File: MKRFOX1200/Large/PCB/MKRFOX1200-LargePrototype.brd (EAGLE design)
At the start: 100 x 100 mm, 195 parts, among them IC2 ARDUINO_MKRFOX1200PROTOPADS, U1 GENERIC-SOIC8, U2 GENERIC-SOIC8, U3 GENERIC-SOIC8, U4 GENERIC-SOIC8

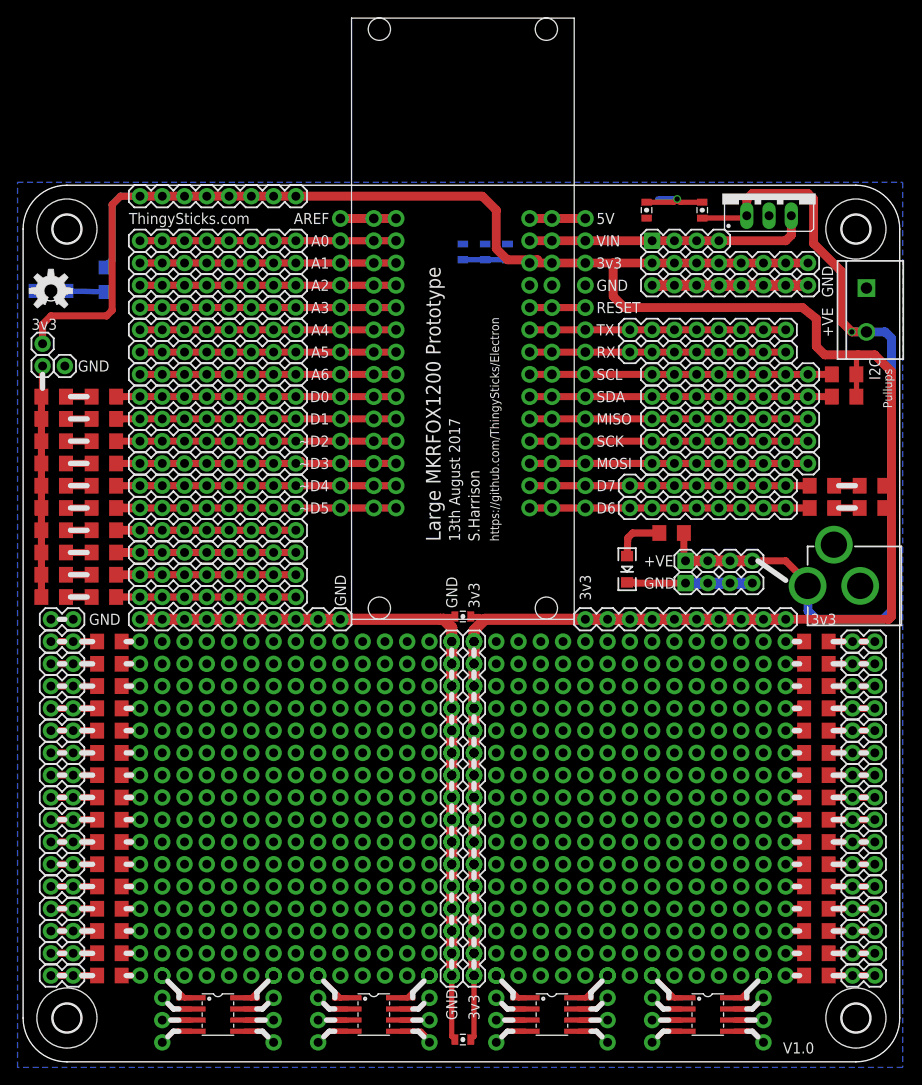
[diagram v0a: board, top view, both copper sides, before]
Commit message: Updated links and name to make it not MKRFox1200 specific as the pinout is the same for WiFi
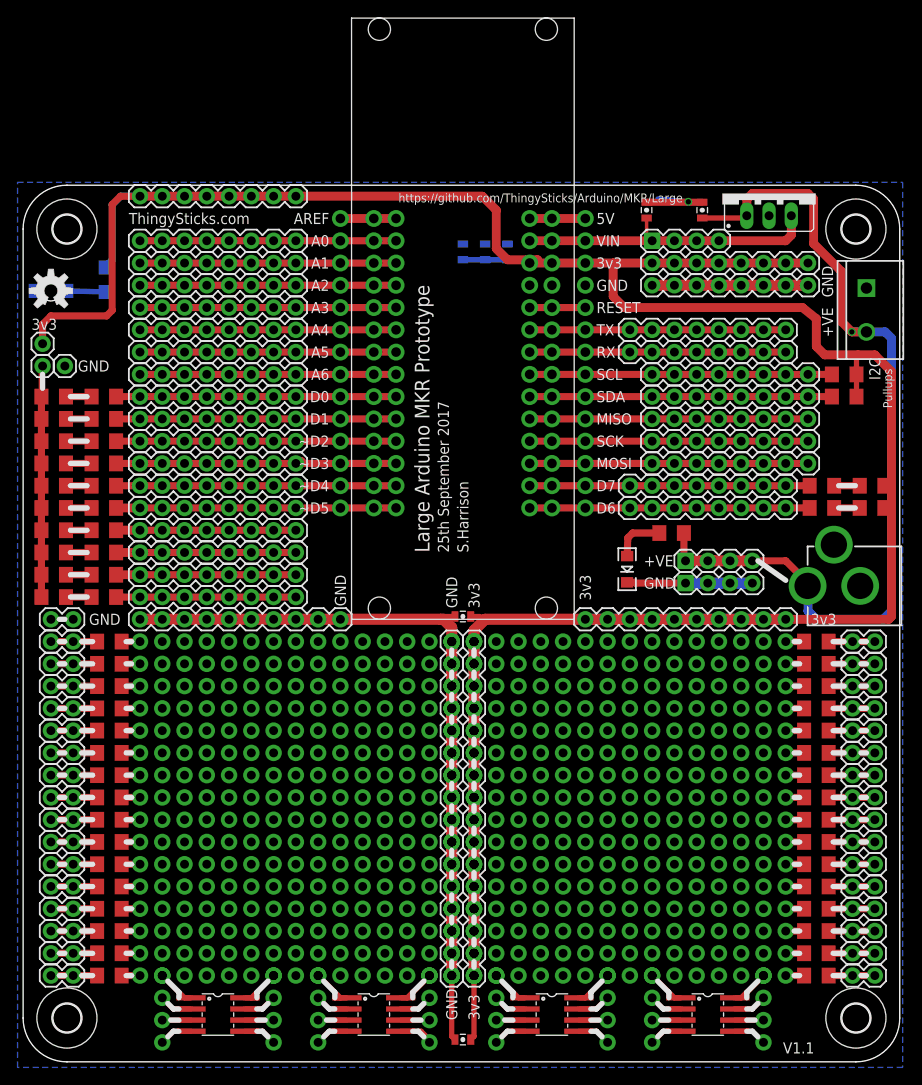
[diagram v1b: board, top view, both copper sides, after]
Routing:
- net GND: track 164.7 -> 167.3 mm
- net VIN: track 32.3 -> 34.9 mm
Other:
- board text added: "25th September 2017"
- board text added: "Large Arduino MKR Prototype"
- board text added: "Large MKR Prototype"
- board text added: "V1.1"
- board text added: "http://ThingySticks.com/Arduino/Prototype/Large"
- board text added: "https://github.com/ThingySticks/Arduino/MKR/Large"
- board text removed: "13th August 2017"
- board text removed: "Large MKRFOX1200 Prototype"
- board text removed: "V1.0"
- board text removed: "https://github.com/ThingySticks/Electron"
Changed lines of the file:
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@@
 <text x="93.0275" y="49.8475" size="1.27" layer="26" font="vector" rot="MR0">3v3</text>
 <text x="12.065" y="95.5675" size="1.27" layer="25" font="vector" ratio="10">ThingySticks.com</text>
-<text x="52.07" y="59.3725" size="1.27" layer="25" font="vector" rot="R90">S.Harrison</text>
-<text x="49.8475" y="59.3725" size="1.27" layer="25" font="vector" rot="R90">13th August 2017</text>
-<text x="47.625" y="59.3725" size="1.6764" layer="25" font="vector" rot="R90">Large MKRFOX1200 Prototype</text>
-<text x="86.6775" y="0.9525" size="1.27" layer="25" font="vector">V1.0</text>
+<text x="50.8" y="58.1025" size="1.27" layer="25" font="vector" rot="R90">S.Harrison</text>
+<text x="48.5775" y="58.1025" size="1.27" layer="25" font="vector" rot="R90">25th September 2017</text>
+<text x="46.355" y="58.1025" size="1.6764" layer="25" font="vector" rot="R90">Large Arduino MKR Prototype</text>
+<text x="86.6775" y="0.9525" size="1.27" layer="25" font="vector">V1.1</text>
 <text x="11.1125" y="51.1175" size="1.27" layer="25" font="vector" rot="R180">GND</text>
 <text x="91.1225" y="86.0425" size="1.27" layer="25" font="vector" rot="R270">+VE</text>
@@
 <wire x1="17.78" y1="7.3025" x2="17.78" y2="7.9375" width="0.6096" layer="25"/>
 <wire x1="17.78" y1="7.9375" x2="16.51" y2="9.2075" width="0.6096" layer="25"/>
-<text x="54.2925" y="59.3725" size="1.016" layer="25" rot="R90">https://github.com/ThingySticks/Electron</text>
+<text x="75.2475" y="99.06" size="1.016" layer="25" rot="R180">https://github.com/ThingySticks/Arduino/MKR/Large</text>
 <wire x1="93.0275" y1="65.7225" x2="94.9325" y2="65.7225" width="0.6096" layer="25"/>
 <wire x1="5.3975" y1="58.1025" x2="7.3025" y2="58.1025" width="0.6096" layer="25"/>
@@
 <wire x1="2.2225" y1="76.835" x2="2.2225" y2="78.4225" width="0.6096" layer="25"/>
 <wire x1="5.3975" y1="55.5625" x2="7.3025" y2="55.5625" width="0.6096" layer="25"/>
-<text x="47.625" y="58.7375" size="1.6764" layer="26" font="vector" rot="MR90">Large MKRFOX1200 Prototype</text>
-<text x="45.4025" y="58.7375" size="1.016" layer="26" rot="MR90">https://github.com/ThingySticks/Electron</text>
+<text x="53.34" y="61.9125" size="1.6764" layer="26" font="vector" rot="MR90">Large MKR Prototype</text>
+<text x="47.3075" y="56.1975" size="1.016" layer="26" rot="MR90">http://ThingySticks.com/Arduino/Prototype/Large</text>
 <wire x1="5.3975" y1="53.0225" x2="7.3025" y2="53.0225" width="0.6096" layer="25"/>
 <text x="98.1075" y="79.0575" size="1.016" layer="25" font="vector" rot="R270">Pullups</text>
@@
 <text x="70.8025" y="56.515" size="1.27" layer="25">+VE</text>
 <text x="70.8025" y="53.975" size="1.27" layer="25">GND</text>
+<text x="44.7675" y="56.1975" size="1.016" layer="26" rot="MR90">https://github.com/ThingySticks/Arduino/MKR/Large</text>
 </plain>
 <attributes>
@@
 <contactref element="IC2" pad="#VIN"/>
 <contactref element="IC2" pad="@VIN"/>
-<wire x1="64.135" y1="93.6625" x2="71.755" y2="93.6625" width="1.016" layer="1"/>
+<wire x1="64.135" y1="93.6625" x2="71.12" y2="93.6625" width="1.016" layer="1"/>
+<wire x1="71.12" y1="93.6625" x2="71.755" y2="93.6625" width="1.016" layer="1"/>
 <wire x1="71.755" y1="93.6625" x2="74.295" y2="93.6625" width="1.016" layer="1"/>
 <wire x1="79.375" y1="93.6625" x2="76.835" y2="93.6625" width="1.016" layer="1"/>
@@
 <wire x1="87.63" y1="94.2975" x2="86.995" y2="93.6625" width="1.016" layer="1"/>
 <wire x1="86.995" y1="93.6625" x2="79.375" y2="93.6625" width="1.016" layer="1"/>
-<wire x1="71.755" y1="93.6625" x2="71.12" y2="96.255" width="0" layer="19" extent="1-1"/>
+<wire x1="71.12" y1="96.255" x2="71.12" y2="93.6625" width="0.4064" layer="1"/>
 </signal>
 <signal name="GND">
@@
 <wire x1="69.7625" y1="54.6975" x2="69.85" y2="54.61" width="0.8128" layer="1"/>
 <wire x1="69.85" y1="54.61" x2="75.565" y2="54.61" width="0.8128" layer="1"/>
-<wire x1="71.12" y1="98.055" x2="74.2425" y2="98.055" width="0.6096" layer="1"/>
-<wire x1="74.2425" y1="98.055" x2="74.6125" y2="98.425" width="0.6096" layer="1"/>
-<via x="74.6125" y="98.425" extent="1-16" drill="0.6"/>
-<wire x1="74.6125" y1="98.425" x2="72.39" y2="98.425" width="0.6096" layer="16"/>
-<wire x1="77.47" y1="98.055" x2="74.9825" y2="98.055" width="0.6096" layer="1"/>
-<wire x1="74.9825" y1="98.055" x2="74.6125" y2="98.425" width="0.6096" layer="1" curve="-90"/>
+<via x="75.8825" y="98.1075" extent="1-16" drill="0.6"/>
+<wire x1="75.8825" y1="98.1075" x2="72.39" y2="98.425" width="0.6096" layer="16"/>
+<wire x1="71.12" y1="98.055" x2="77.47" y2="98.055" width="0.8128" layer="1"/>
+<wire x1="75.8825" y1="98.1075" x2="77.47" y2="98.1075" width="0.4064" layer="1"/>
+<wire x1="77.47" y1="98.1075" x2="77.47" y2="98.055" width="0.4064" layer="1"/>
 </signal>
 <signal name="3.3V">
